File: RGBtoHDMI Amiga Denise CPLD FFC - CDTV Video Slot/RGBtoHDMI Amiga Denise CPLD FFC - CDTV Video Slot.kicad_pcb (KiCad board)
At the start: 2 copper layers, 94 x 121.6 mm, 33 parts, among them CN10 Conn_02x15_Odd_Even, J1 Raspberry_Pi_2_3, U1 XC9572VQ44 or XC9572XL-10VQG4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

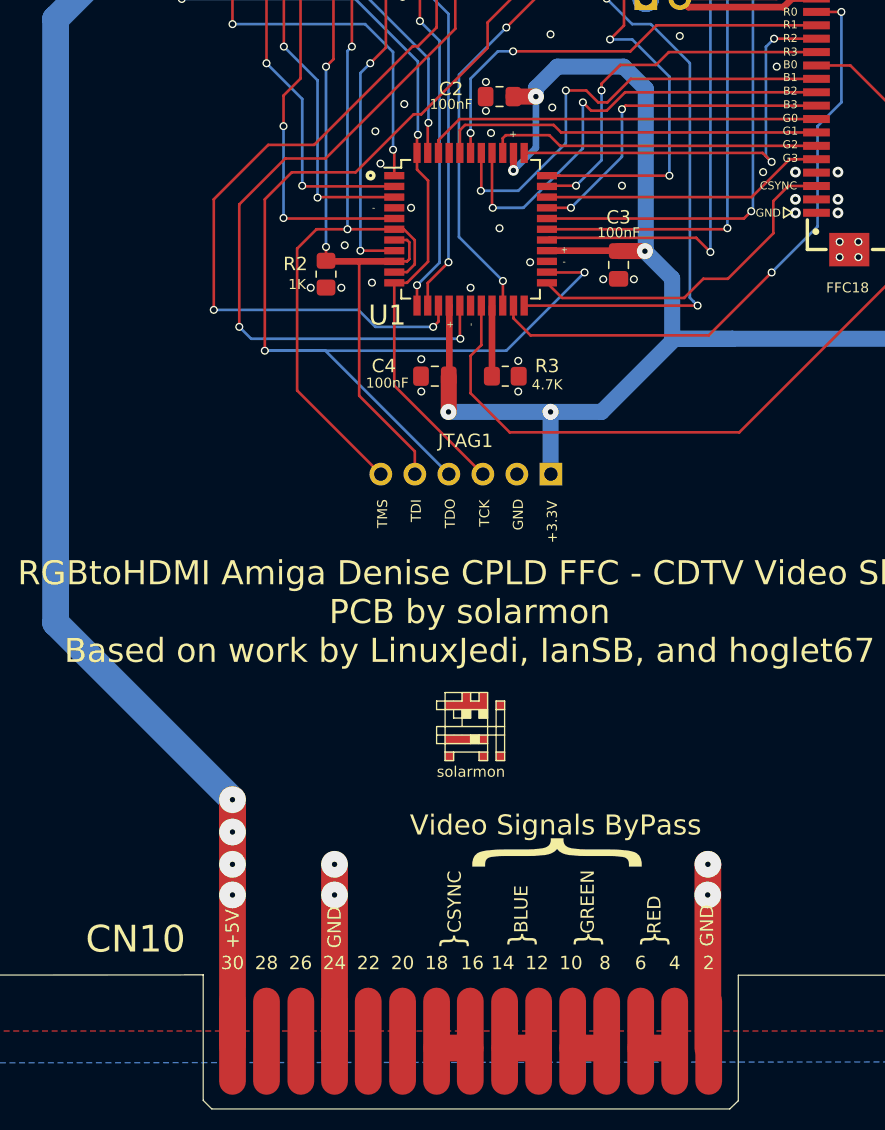
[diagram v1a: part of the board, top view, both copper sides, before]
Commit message: Added L+R audio points
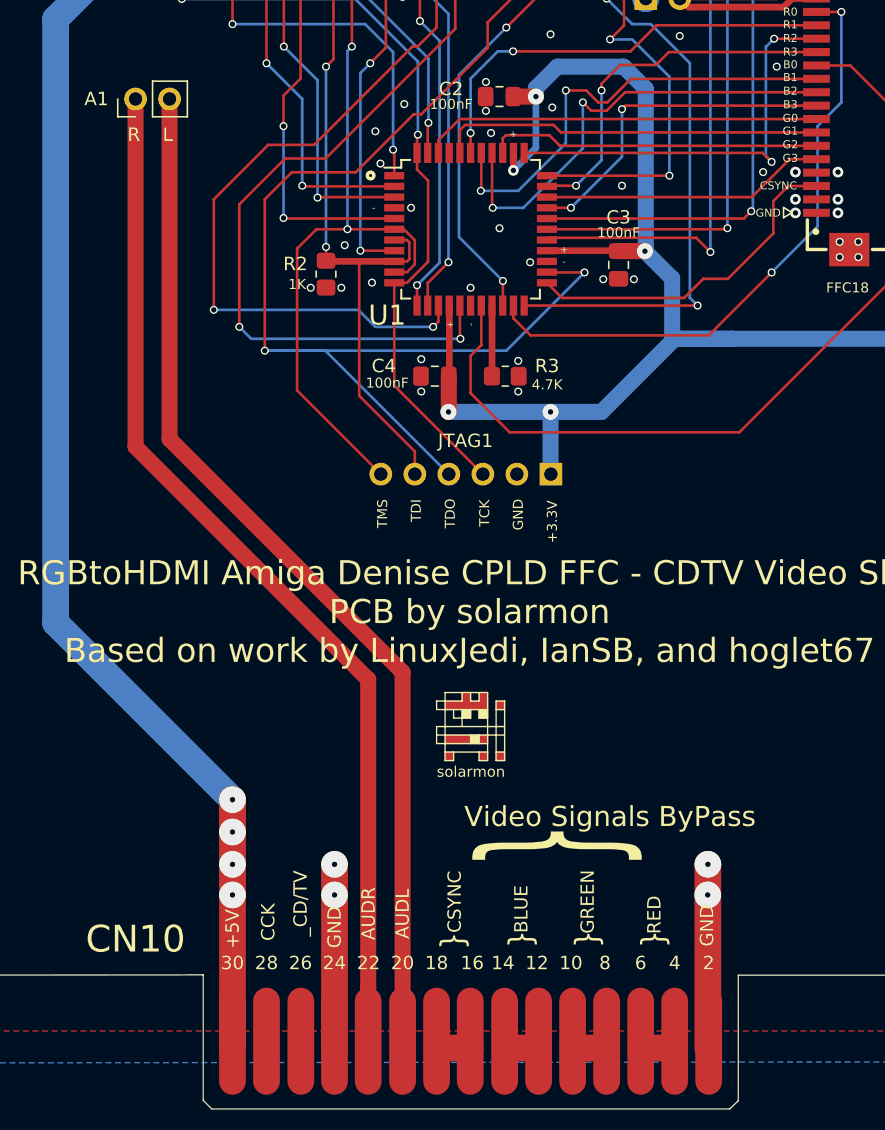
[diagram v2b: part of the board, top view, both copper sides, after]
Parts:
- added A1: Conn_01x02, Connector_PinHeader_2.54mm:PinHeader_1x02_P2.54mm_Vertical, F.Cu at (71.1, 83.8)
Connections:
- CN10 pad 20: Net-(CN10-Pad20) -> AUDL
- CN10 pad 22: Net-(CN10-Pad22) -> AUDR
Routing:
- net AUDL: track 0.00 -> 77.6 mm
- net AUDR: track 0.00 -> 77.6 mm
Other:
- board text added: "AUDL"
- board text added: "AUDR"
- board text added: "CCK"
- board text added: "L"
- board text added: "R"
- board text added: "_CD/TV"
